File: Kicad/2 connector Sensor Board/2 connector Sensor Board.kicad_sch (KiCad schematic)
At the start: 11 parts, among them J1 SPI, J15 TE 3-2363962-0 Connector, J2 7 pin FPC 0.3mm Panasonic Y3b, J3 free pins, J4 TE 3-2363962-0 Connector, J5 7 pin FPC 0.3mm Panasonic Y3b, J7 JST SH

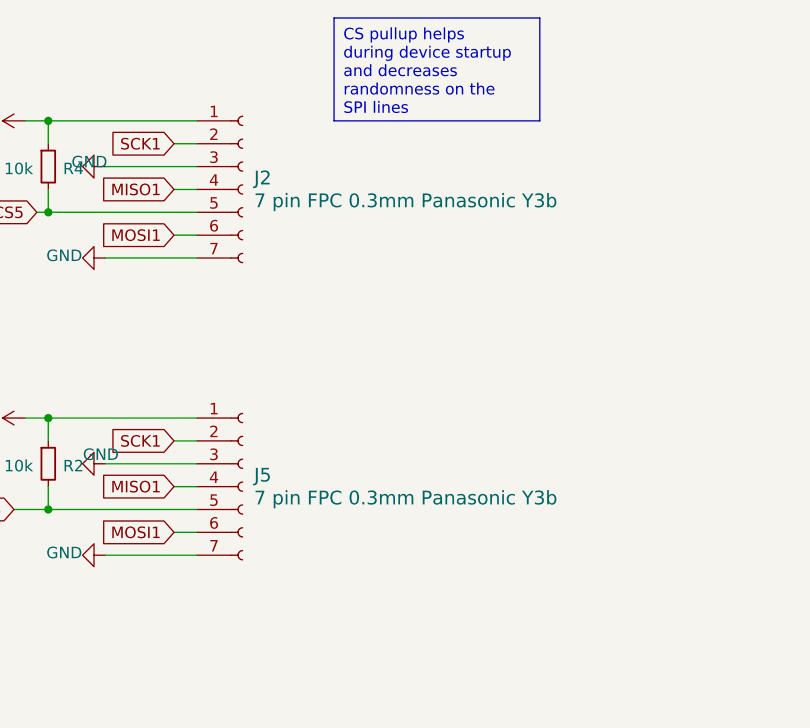
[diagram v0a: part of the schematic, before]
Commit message: Added LCSC part numbers, DNP attr, and exported Gerbers
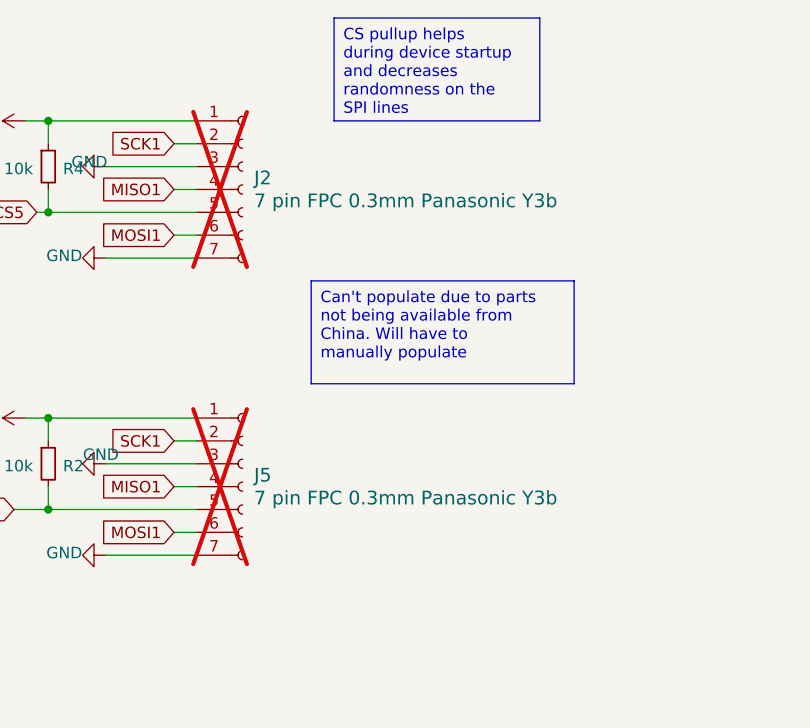
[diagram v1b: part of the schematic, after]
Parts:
- J15, J4: LCSC (none) -> C425104
- J2, J5: now not fitted
- J7: LCSC (none) -> C160404
- R2, R4: LCSC (none) -> C25744
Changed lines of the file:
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@@
 		)
 	)
+	(text_box "Can't populate due to parts not being available from China. Will have to manually populate"
+		(exclude_from_sim no)
+		(at 96.52 45.72 0)
+		(size 29.21 11.43)
+		(stroke
+			(width 0)
+			(type default)
+		)
+		(fill
+			(type none)
+		)
+		(effects
+			(font
+				(size 1.27 1.27)
+			)
+			(justify left top)
+		)
+	)
 	(text_box "CS pullup helps during device startup and decreases randomness on the SPI lines"
 		(exclude_from_sim no)
@@
 			)
 		)
+		(property "LCSC" "C25744"
+			(at 70.104 66.294 0)
+			(effects
+				(font
+					(size 1.27 1.27)
+				)
+				(hide yes)
+			)
+		)
 		(pin "2"
 		)
@@
 			)
 		)
+		(property "LCSC" "C160404"
+			(at 172.72 35.9155 0)
+			(effects
+				(font
+					(size 1.27 1.27)
+				)
+				(hide yes)
+			)
+		)
 		(pin "MP"
 		)
@@
 			)
 		)
+		(property "LCSC" "C425104"
+			(at 195.326 93.472 0)
+			(effects
+				(font
+					(size 1.27 1.27)
+				)
+				(hide yes)
+			)
+		)
 		(pin "28"
 		)
@@
 			)
 		)
+		(property "LCSC" "C425104"
+			(at 255.016 93.472 0)
+			(effects
+				(font
+					(size 1.27 1.27)
+				)
+				(hide yes)
+			)
+		)
 		(pin "28"
 		)
@@
 		(in_bom yes)
 		(on_board yes)
-		(dnp no)
+		(dnp yes)
 		(fields_autoplaced yes)
 		(property "Reference" "J5"
@@
 		(in_bom yes)
 		(on_board yes)
-		(dnp no)
+		(dnp yes)
 		(fields_autoplaced yes)
 		(property "Reference" "J2"
@@
 			(effects
 				(font
+					(size 1.27 1.27)
+				)
+				(hide yes)
+			)
+		)
+		(property "LCSC" "C25744"
+			(at 70.104 33.274 0)
+			(effects
+				(font
